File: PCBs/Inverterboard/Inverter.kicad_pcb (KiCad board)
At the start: 2 copper layers, 43 parts, among them IC1 L6494LDTR, J1 43045-0406, J2 43045-0406, J3 43045-0406, J4 43045-0406, U1 IPT015N10N5ATMA1, U2 IPT015N10N5ATMA1, U3 IPT015N10N5ATMA1, U4 IPT015N10N5ATMA1

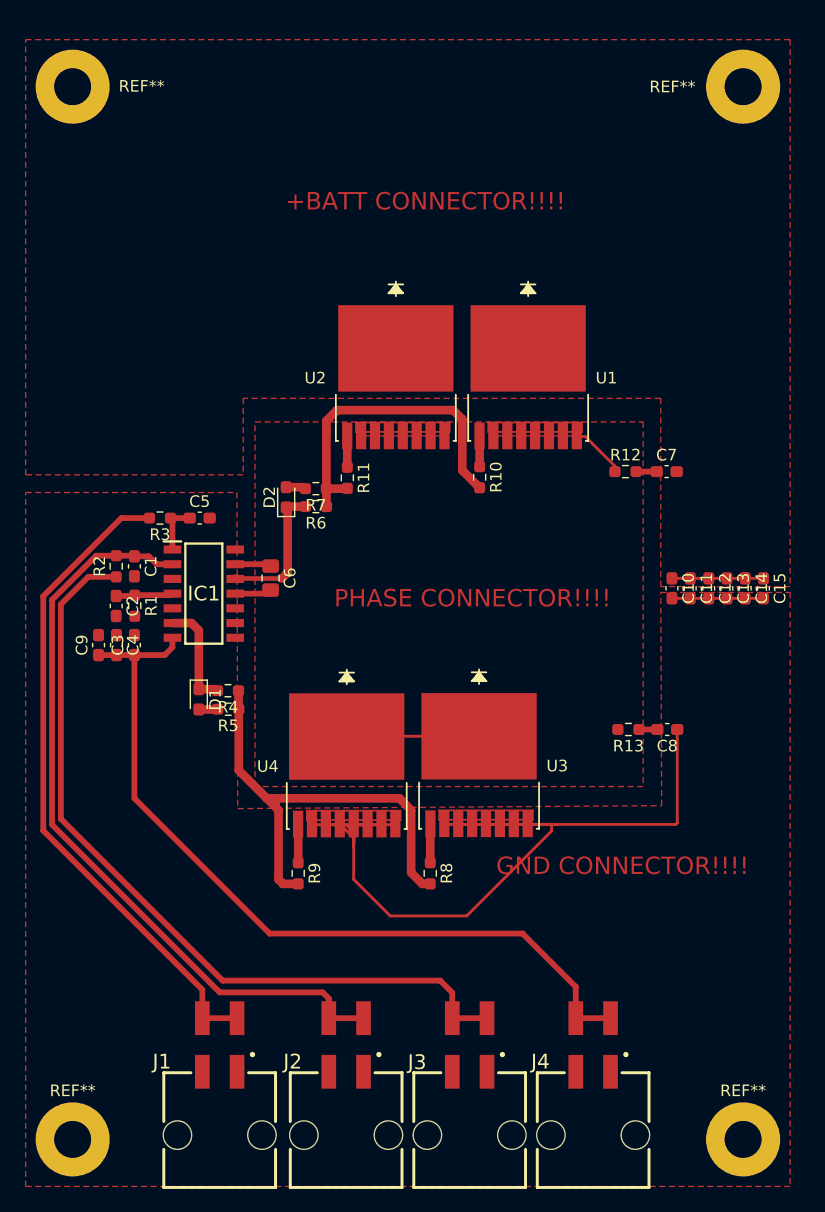
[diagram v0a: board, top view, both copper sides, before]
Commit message: Merged PCB with changes from Jakob. Added FOC overview.
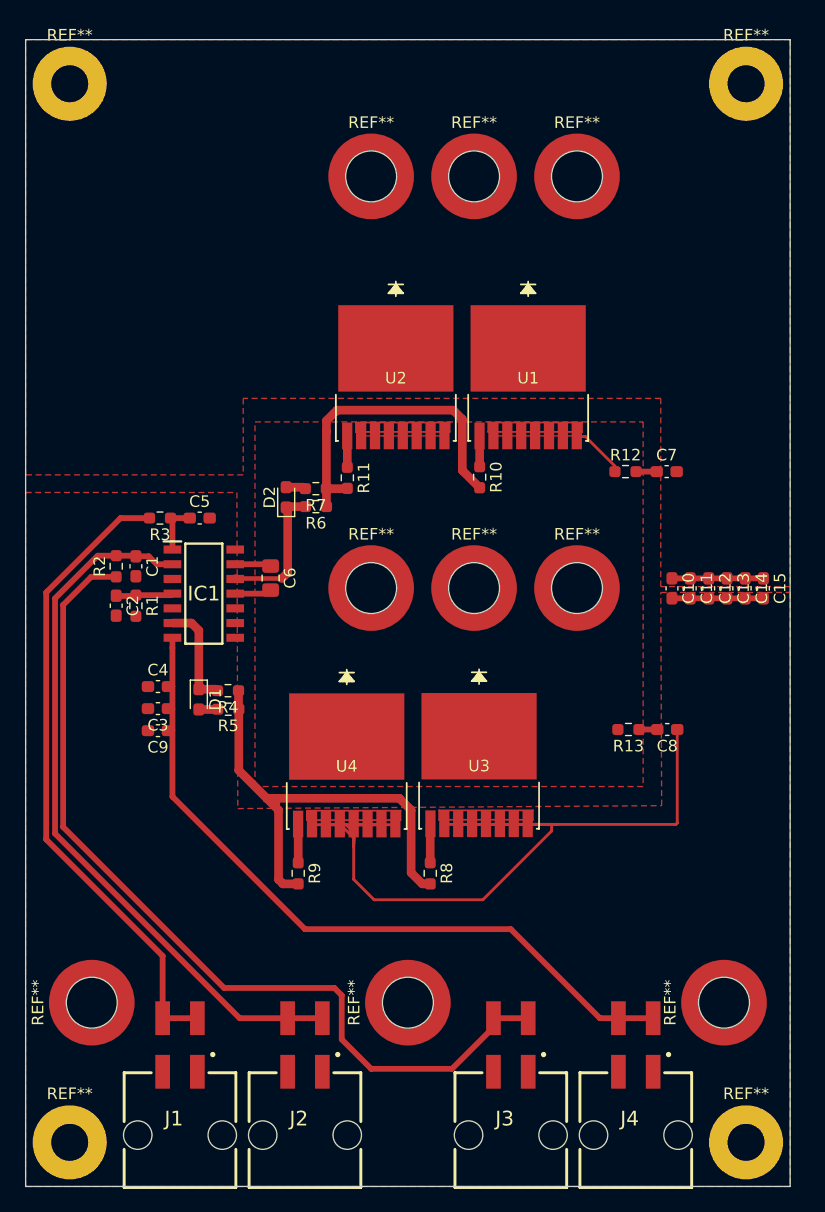
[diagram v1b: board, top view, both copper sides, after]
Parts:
- removed the REF** at (130.6, 49.8)
- removed the REF** at (130.6, 140.7)
- added REF**: Mounting_Wuerth_WA-SMSR-M3_H2.6mm_ReverseMount_9775026360, Mounting_Wuerth:Mounting_Wuerth_WA-SMSR-M3_H2.6mm_ReverseMount_9775026360, F.Cu at (116.2, 57.5)
- added REF**: MountingHole_3.2mm_M3_Pad, MountingHole:MountingHole_3.2mm_M3_Pad, F.Cu at (130.8, 49.5)
- added REF**: MountingHole_3.2mm_M3_Pad, MountingHole:MountingHole_3.2mm_M3_Pad, F.Cu at (130.8, 141.0)
- added REF**: Mounting_Wuerth_WA-SMSR-M3_H2.6mm_ReverseMount_9775026360, Mounting_Wuerth:Mounting_Wuerth_WA-SMSR-M3_H2.6mm_ReverseMount_9775026360, F.Cu at (107.3, 57.5)
- added REF**: Mounting_Wuerth_WA-SMSR-M3_H2.6mm_ReverseMount_9775026360, Mounting_Wuerth:Mounting_Wuerth_WA-SMSR-M3_H2.6mm_ReverseMount_9775026360, F.Cu at (116.2, 93.1)
- added REF**: Mounting_Wuerth_WA-SMSR-M3_H2.6mm_ReverseMount_9775026360, Mounting_Wuerth:Mounting_Wuerth_WA-SMSR-M3_H2.6mm_ReverseMount_9775026360, F.Cu at (107.3, 93.1)
- added REF**: Mounting_Wuerth_WA-SMSR-M3_H2.6mm_ReverseMount_9775026360, Mounting_Wuerth:Mounting_Wuerth_WA-SMSR-M3_H2.6mm_ReverseMount_9775026360, F.Cu at (128.9, 128.9)
- added REF**: Mounting_Wuerth_WA-SMSR-M3_H2.6mm_ReverseMount_9775026360, Mounting_Wuerth:Mounting_Wuerth_WA-SMSR-M3_H2.6mm_ReverseMount_9775026360, F.Cu at (101.6, 128.9)
- added REF**: Mounting_Wuerth_WA-SMSR-M3_H2.6mm_ReverseMount_9775026360, Mounting_Wuerth:Mounting_Wuerth_WA-SMSR-M3_H2.6mm_ReverseMount_9775026360, F.Cu at (74.3, 128.9)
- added REF**: Mounting_Wuerth_WA-SMSR-M3_H2.6mm_ReverseMount_9775026360, Mounting_Wuerth:Mounting_Wuerth_WA-SMSR-M3_H2.6mm_ReverseMount_9775026360, F.Cu at (98.4, 93.1)
- added REF**: Mounting_Wuerth_WA-SMSR-M3_H2.6mm_ReverseMount_9775026360, Mounting_Wuerth:Mounting_Wuerth_WA-SMSR-M3_H2.6mm_ReverseMount_9775026360, F.Cu at (98.4, 57.5)
- moved C9 9.00 mm to (80.0, 105.4), turned to 180 degrees
- moved C3 5.85 mm to (80.0, 103.5), turned to 180 degrees
- moved C4 5.07 mm to (80.0, 101.6), turned to 0 degrees
- moved J4 3.68 mm to (121.3, 134.9)
- moved J2 3.56 mm to (92.7, 134.9)
- moved J3 3.56 mm to (110.5, 134.9)
- moved J1 3.43 mm to (81.9, 134.9)
- moved REF** 0.36 mm to (72.4, 49.5)
- moved REF** 0.36 mm to (72.4, 141.0)
- moved C1 0.13 mm to (78.1, 91.2)
- moved R1 0.10 mm to (78.1, 94.6)
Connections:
- net Net-(C10-Pad1) renamed +BATT
- net Net-(C6-Pad2) renamed PHASE
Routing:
- net PHASE: track 41.2 -> 23.3 mm
- net +5V: track 69.5 -> 78.1 mm
- net +12V: track 70.4 -> 64.4 mm
- net Enable: track 66.5 -> 62.0 mm
- net PWM: track 57.1 -> 55.5 mm
- net +BATT: track 7.90 -> 9.39 mm
- net GND: track 106.4 -> 105.2 mm
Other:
- board outline added: 66 x 99.1 mm
- board text removed: "+BATT CONNECTOR!!!!"
- board text removed: "GND CONNECTOR!!!!"
- board text removed: "PHASE CONNECTOR!!!!"

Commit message: Changed mini-fits to pin headers
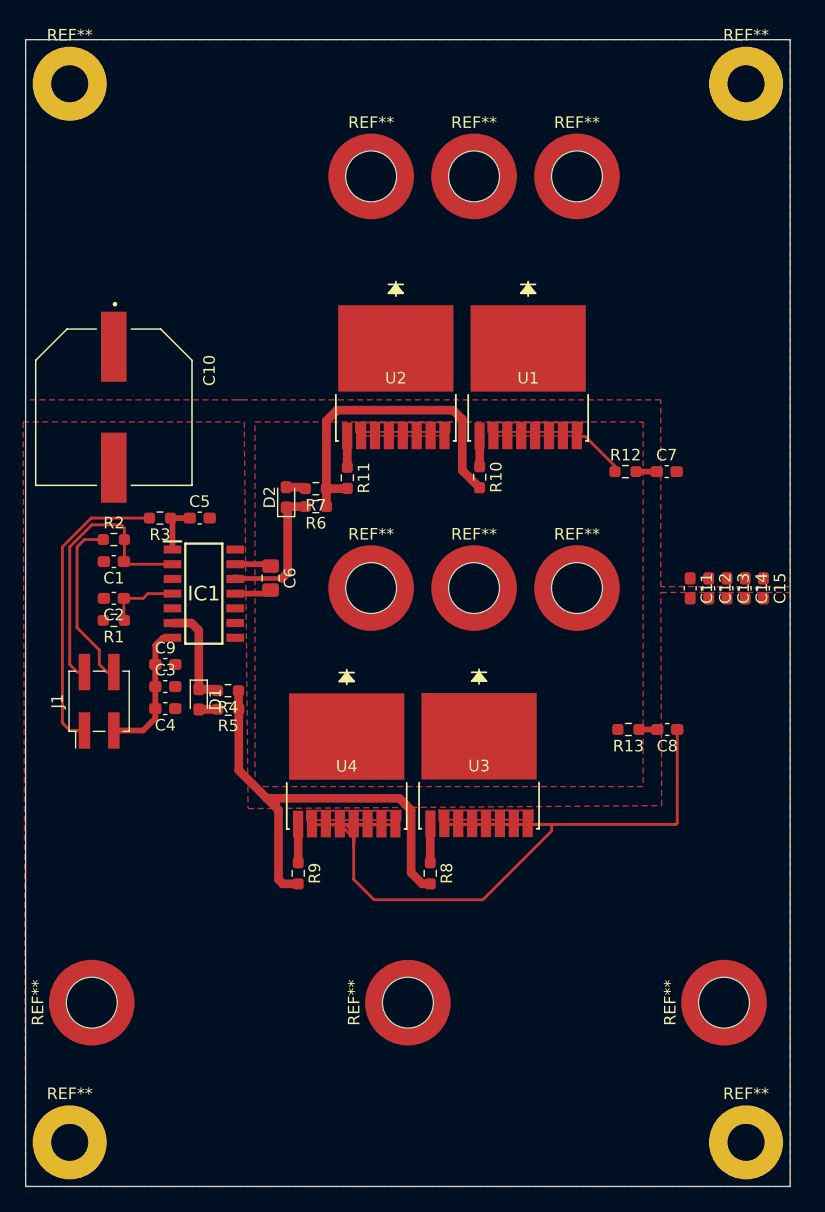
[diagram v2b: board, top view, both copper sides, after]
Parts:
- removed J2, J3, J4: 43045-0406, ElectricGoKart:43045-0406
- C10: footprint Capacitor_SMD:C_0603_1608Metric_Pad1.08x0.95mm_HandSolder -> EEE-TKK101UAQ:CAPAE1350X1400N
- C11: value 10µ -> 4.7µ
- C4: value 100µ -> 100n
- J1: value 43045-0406 -> Conn_02x02_Odd_Even; footprint ElectricGoKart:43045-0406 -> Connector_PinHeader_2.54mm:PinHeader_2x02_P2.54mm_Vertical_SMD
- moved C10 50.7 mm to (76.2, 77.5)
- moved J1 32.8 mm to (74.9, 102.9), turned to 90 degrees
- moved C9 5.75 mm to (80.6, 99.7), turned to 0 degrees
- moved R2 2.32 mm to (76.2, 88.9), turned to 0 degrees
- moved R1 2.29 mm to (76.2, 95.9), turned to 180 degrees
- moved C3 2.01 mm to (80.6, 101.6), turned to 0 degrees
- moved C4 2.01 mm to (80.6, 103.5), turned to 180 degrees
- moved C1 1.95 mm to (76.2, 90.8), turned to 180 degrees
- moved C2 0.67 mm to (76.2, 94.0), turned to 180 degrees
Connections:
- J1 pad 1: GND -> PWM
- J1 pad 2: GND -> Enable
- J1 pad 3: PWM -> +12V
- J1 pad 4: PWM -> +5V
- U1 pad 2: Net-(U1-Pad2) -> PHASE
- U1 pad 3: Net-(U1-Pad3) -> PHASE
- U2 pad 2: Net-(U2-Pad2) -> PHASE
- U2 pad 3: Net-(U2-Pad3) -> PHASE
- U3 pad 2: Net-(U3-Pad2) -> GND
- U3 pad 3: Net-(U3-Pad3) -> GND
- U4 pad 2: Net-(U4-Pad2) -> GND
- U4 pad 3: Net-(U4-Pad3) -> GND
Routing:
- net +5V: track 78.1 -> 15.0 mm
- net +12V: track 64.4 -> 12.1 mm
- net Enable: track 62.0 -> 24.5 mm
- net PWM: track 55.5 -> 25.9 mm
- net GND: track 105.2 -> 97.3 mm
- net +BATT: track 9.39 -> 1.50 mm
- net Net-(C2-Pad1): track 4.94 -> 6.29 mm

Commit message: Changed ceramic DC-link cap footprint size
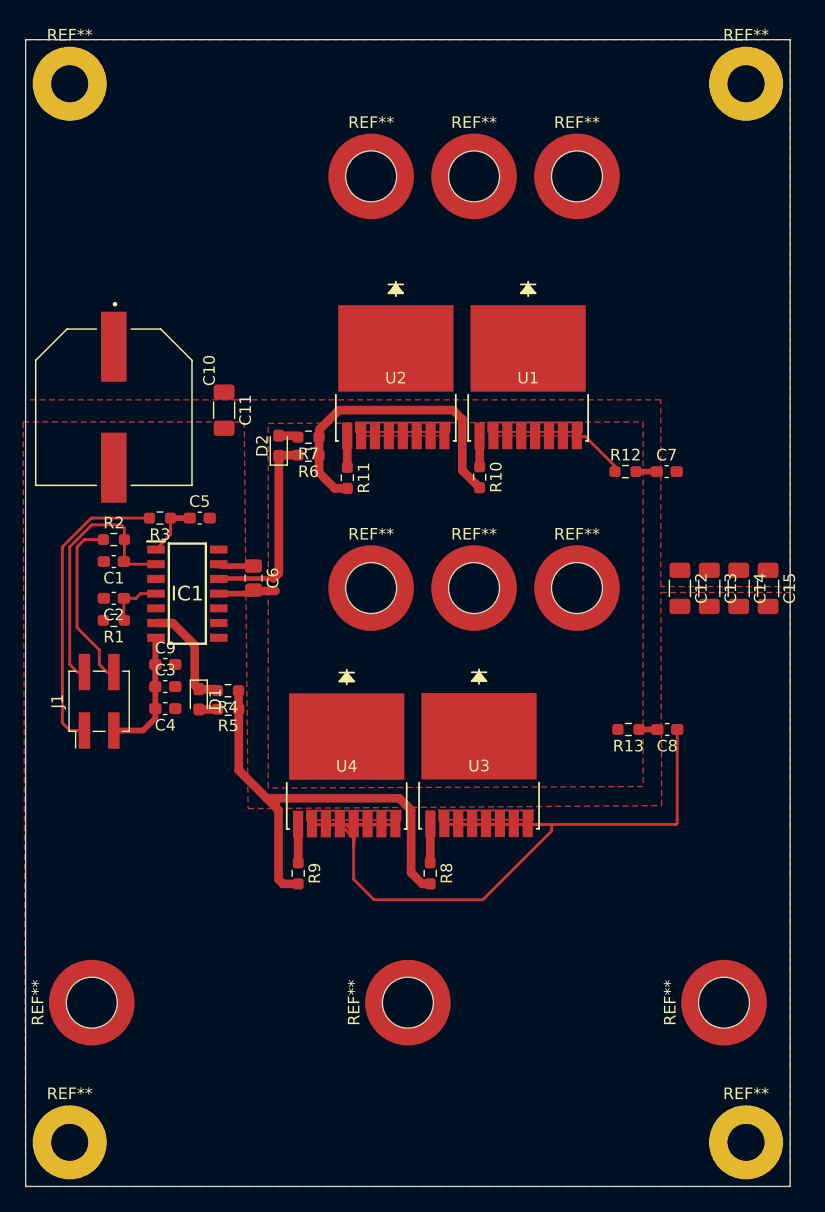
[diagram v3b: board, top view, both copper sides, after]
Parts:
- C11, C12, C13, C14, C15: footprint Capacitor_SMD:C_0603_1608Metric_Pad1.08x0.95mm_HandSolder -> Capacitor_SMD:C_1206_3216Metric_Pad1.33x1.80mm_HandSolder
- REF** (x9): value Mounting_Wuerth_WA-SMSR-M3_H2.6mm_ReverseMount_9775026360 -> Mounting_Wuerth_WA-SMSI-M3_H15mm_9774150360; footprint Mounting_Wuerth:Mounting_Wuerth_WA-SMSR-M3_H2.6mm_ReverseMount_9775026360 -> Mounting_Wuerth:Mounting_Wuerth_WA-SMSI-M3_H15mm_9774150360
- moved C11 43.1 mm to (85.7, 77.7)
- moved D2 4.49 mm to (90.4, 80.8)
- moved R6 4.49 mm to (93.0, 81.6)
- moved R7 4.49 mm to (93.0, 80.1)
- moved C12 2.49 mm to (125.1, 93.1)
- moved C13 1.52 mm to (127.6, 93.1)
- moved C6 1.47 mm to (88.3, 92.2)
- moved IC1 1.42 mm to (82.5, 93.6)
- moved C14 0.56 mm to (130.2, 93.1)
- moved C15 0.41 mm to (132.7, 93.1)
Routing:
- net Net-(D2-Pad1): track 12.1 -> 17.2 mm
- net PHASE: track 23.3 -> 25.0 mm
- net Enable: track 24.5 -> 23.1 mm
- net Net-(C2-Pad1): track 6.29 -> 4.87 mm
- net Net-(R10-Pad2): track 28.2 -> 26.9 mm
- net +12V: track 12.1 -> 11.0 mm
- net Net-(C5-Pad1): track 4.44 -> 5.12 mm

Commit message: Last fixes after PCB review
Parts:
- removed the REF** at (98.4, 57.5)
- removed the REF** at (72.4, 49.5)
- removed the REF** at (130.8, 49.5)
- removed the REF** at (130.8, 141.0)
- removed the REF** at (72.4, 141.0)
- removed the REF** at (107.3, 57.5)
- removed the REF** at (116.2, 57.5)
- removed the REF** at (98.4, 93.1)
- removed the REF** at (107.3, 93.1)
- removed the REF** at (116.2, 93.1)
- removed the REF** at (128.9, 128.9)
- removed the REF** at (101.6, 128.9)
- removed the REF** at (74.3, 128.9)
- added C16: 4.7µ, Capacitor_SMD:C_1206_3216Metric_Pad1.33x1.80mm_HandSolder, F.Cu at (76.7, 77.7)
- added C17: 4.7µ, Capacitor_SMD:C_1206_3216Metric_Pad1.33x1.80mm_HandSolder, F.Cu at (82.7, 77.7)
- added C18: 4.7µ, Capacitor_SMD:C_1206_3216Metric_Pad1.33x1.80mm_HandSolder, F.Cu at (73.7, 77.7)
- added C19: 4.7µ, Capacitor_SMD:C_1206_3216Metric_Pad1.33x1.80mm_HandSolder, F.Cu at (70.6, 77.7)
- added REF**: MountingHole_3.2mm_M3_Pad, MountingHole:MountingHole_3.2mm_M3_Pad, F.Cu at (118.1, 106.0)
- added REF**: MountingHole_3.2mm_M3_Pad, MountingHole:MountingHole_3.2mm_M3_Pad, F.Cu at (79.0, 62.2)
- added REF**: MountingHole_3.2mm_M3_Pad, MountingHole:MountingHole_3.2mm_M3_Pad, F.Cu at (124.2, 62.2)
- added REF**: MountingHole_3.2mm_M3_Pad, MountingHole:MountingHole_3.2mm_M3_Pad, F.Cu at (114.3, 125.1)
- added REF**: MountingHole_3.2mm_M3_Pad, MountingHole:MountingHole_3.2mm_M3_Pad, F.Cu at (88.9, 125.1)
- added U**: 7466203R, KiCad:7466203R, F.Cu at (128.9, 125.1)
- added U**: 7466203R, KiCad:7466203R, F.Cu at (101.6, 125.1)
- added U**: 7466203R, KiCad:7466203R, F.Cu at (74.3, 125.1)
- added U**: 7466203R, KiCad:7466203R, F.Cu at (116.2, 93.1)
- added U**: 7466203R, KiCad:7466203R, F.Cu at (107.3, 93.1)
- added U**: 7466203R, KiCad:7466203R, F.Cu at (98.4, 93.1)
- added U**: 7466203R, KiCad:7466203R, F.Cu at (116.2, 62.4)
- added U**: 7466203R, KiCad:7466203R, F.Cu at (107.3, 62.4)
- added U**: 7466203R, KiCad:7466203R, F.Cu at (98.4, 62.4)
- C10: value 100µ -> 4.7µ; footprint EEE-TKK101UAQ:CAPAE1350X1400N -> Capacitor_SMD:C_1206_3216Metric_Pad1.33x1.80mm_HandSolder
- C7, C8: footprint Capacitor_SMD:C_0603_1608Metric_Pad1.08x0.95mm_HandSolder -> Capacitor_SMD:C_1206_3216Metric_Pad1.33x1.80mm_HandSolder
- R12, R13: footprint Resistor_SMD:R_0603_1608Metric_Pad0.98x0.95mm_HandSolder -> Resistor_SMD:R_1206_3216Metric_Pad1.30x1.75mm_HandSolder
- moved R13 5.65 mm to (121.3, 99.7), turned to 90 degrees
- moved C8 5.63 mm to (124.5, 99.7), turned to 270 degrees
- moved C7 3.71 mm to (124.6, 79.4), turned to 270 degrees
- moved R12 3.68 mm to (120.8, 79.4), turned to 90 degrees
- moved C10 3.44 mm to (79.6, 77.7)
- moved R11 1.52 mm to (94.9, 83.3), turned to 180 degrees
- moved R10 1.21 mm to (107.1, 82.5), turned to 180 degrees
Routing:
- net GND: track 97.3 -> 41.6 mm
- net Net-(R10-Pad2): track 26.9 -> 21.2 mm
- net PHASE: track 25.0 -> 22.7 mm
- net Net-(C7-Pad1): track 1.78 -> 3.82 mm
- net Net-(C8-Pad2): track 1.58 -> 3.18 mm
- net Net-(R11-Pad1): track 2.71 -> 3.62 mm
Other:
- board size 66 x 99.1 mm -> 66 x 71.8 mm

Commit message: Created gerber files
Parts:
- removed the U** at (116.2, 93.1)
- removed the U** at (98.4, 93.1)
- removed the U** at (98.4, 62.4)
- added U**: 7466203R, KiCad:7466203R, F.Cu at (117.5, 93.1)
- added U**: 7466203R, KiCad:7466203R, F.Cu at (97.2, 93.1)
- added U**: 7466203R, KiCad:7466203R, F.Cu at (94.5, 62.4)
- moved U** 2.67 mm to (104.6, 62.4)
- moved C8 1.40 mm to (124.5, 101.1)
- moved R13 1.40 mm to (121.3, 101.1)
- moved U** 1.40 mm to (114.8, 62.4)
- moved REF** 0.64 mm to (118.1, 106.7)
